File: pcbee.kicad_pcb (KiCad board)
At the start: 2 copper layers, 50.8 x 43.2 mm, 5 parts

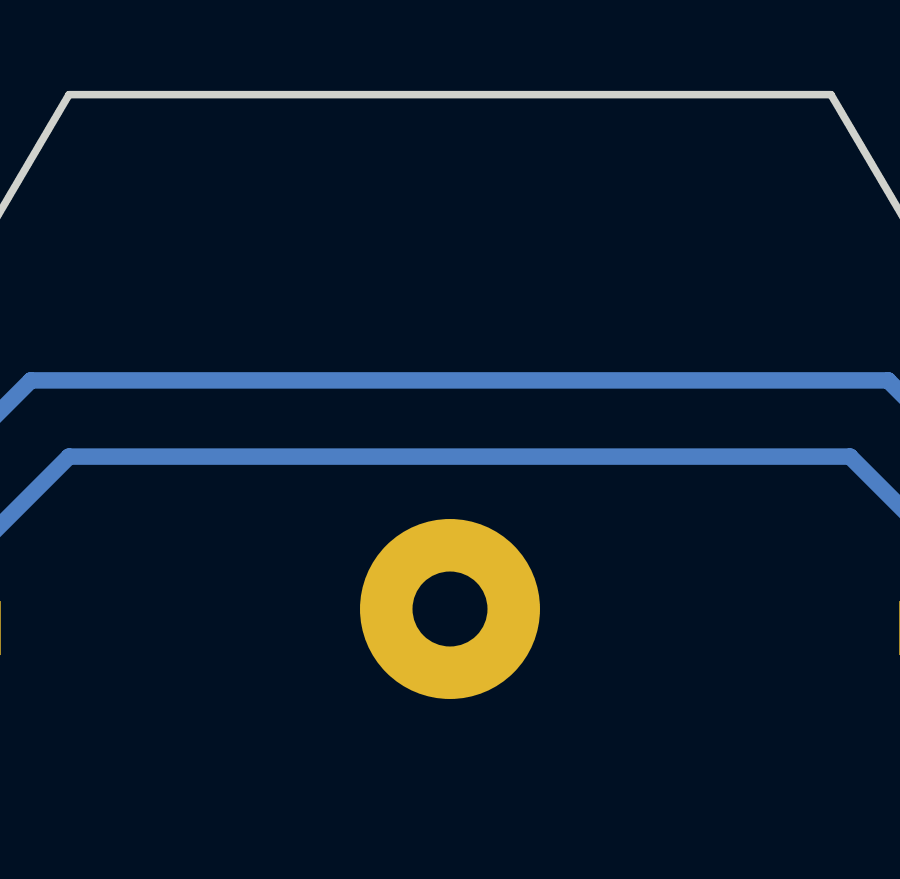
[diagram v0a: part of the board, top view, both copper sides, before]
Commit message: move mounting hole
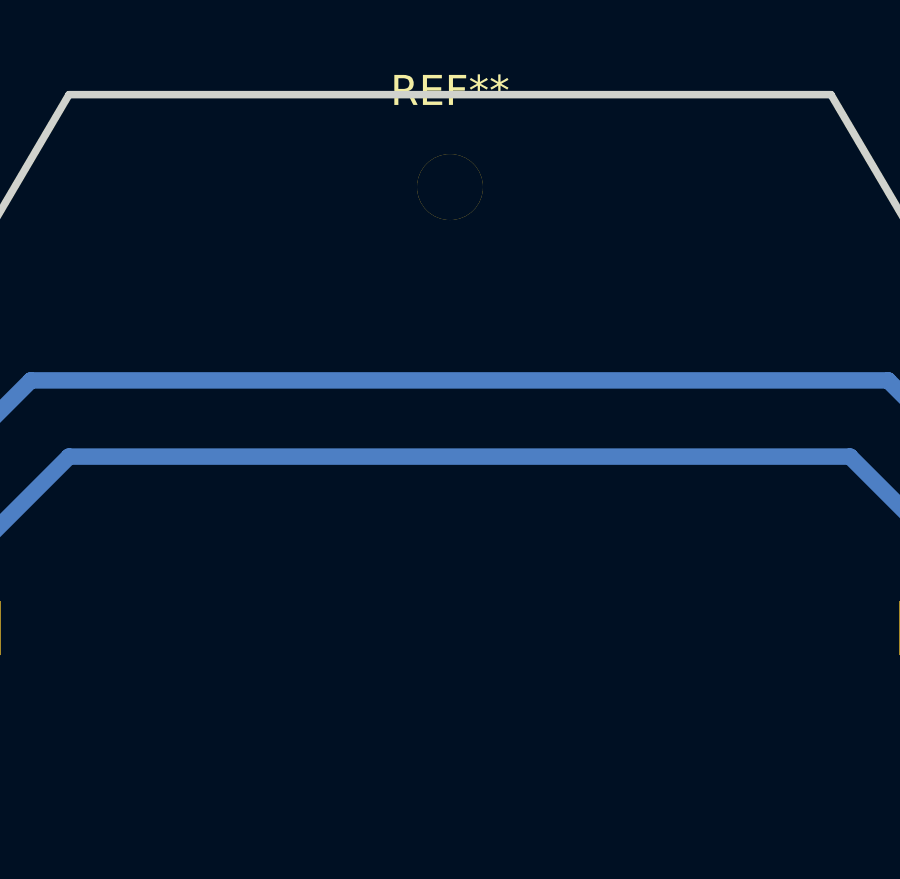
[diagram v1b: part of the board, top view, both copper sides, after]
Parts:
- removed the REF** at (149.9, 92.1)
- added REF**: MountingHole_2.2mm_M2_Pad, Mounting_Holes:MountingHole_2.2mm_M2_Pad, F.Cu at (149.9, 78.0)
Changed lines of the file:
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@@
-(kicad_pcb (version 4) (host pcbnew 4.0.7+dfsg1-1)
+(kicad_pcb (version 4) (host pcbnew 4.0.7)
   (general
     (links 4)
     (no_connects 0)
-    (area 124.334999 74.804999 175.385001 119.485)
+    (area 124.334999 74.804999 175.385001 118.235001)
     (thickness 1.6)
     (drawings 8)
@@
     (34 B.Paste user hide)
     (35 F.Paste user)
-    (36 B.SilkS user hide)
+    (36 B.SilkS user)
     (37 F.SilkS user)
-    (38 B.Mask user hide)
-    (39 F.Mask user hide)
+    (38 B.Mask user)
+    (39 F.Mask user)
     (40 Dwgs.User user hide)
     (41 Cmts.User user hide)
@@
     (mod_text_size 1 1)
     (mod_text_width 0.15)
-    (pad_size 1.524 1.524)
-    (pad_drill 0.762)
+    (pad_size 2.2 2.2)
+    (pad_drill 2.2)
     (pad_to_mask_clearance 0.2)
     (aux_axis_origin 0 0)
-    (visible_elements FFFF3F1F)
+    (visible_elements FFFF7F9F)
     (pcbplotparams
       (layerselection 0x010f0_80000001)
@@
       (xy 0.536977 -4.539402) (xy 0.697932 -4.645079) (xy 0.864099 -4.626846)) (layer F.Mask) (width 0.01))
   )
-  (module Wire_Pads:SolderWirePad_single_2-5mmDrill (layer F.Cu)
-    (at 149.86 92.075)
-    (fp_text reference REF** (at 0 -5.08) (layer F.SilkS) hide
+  (module Mounting_Holes:MountingHole_2.2mm_M2_Pad (layer F.Cu)
+    (at 149.86 78.01)
+    (descr "Mounting Hole 2.2mm, M2")
+    (tags "mounting hole 2.2mm m2")
+    (attr virtual)
+    (fp_text reference REF** (at 0 -3.2) (layer F.SilkS)
       (effects (font (size 1 1) (thickness 0.15)))
     )
-    (fp_text value SolderWirePad_single_2-5mmDrill (at 1.27 5.08) (layer F.Fab)
+    (fp_text value MountingHole_2.2mm_M2_Pad (at 0 3.2) (layer F.Fab)
       (effects (font (size 1 1) (thickness 0.15)))
     )
-    (pad 1 thru_hole circle (at 0 0) (size 5.99948 5.99948) (drill 2.49936) (layers *.Cu *.Mask))
+    (fp_text user %R (at 0.3 0) (layer F.Fab)
+      (effects (font (size 1 1) (thickness 0.15)))
+    )
+    (fp_circle (center 0 0) (end 2.2 0) (layer Cmts.User) (width 0.15))
+    (fp_circle (center 0 0) (end 2.45 0) (layer F.CrtYd) (width 0.05))
+    (pad 1 thru_hole circle (at 0 0) (size 2.2 2.2) (drill 2.2) (layers *.Cu *.Mask))
   )
   (gr_text "PRODUCTION ID\nMUST BE ON\nTHIS (BACK) SILK" (at 150.495 99.695) (layer B.Fab)
     (effects (font (size 1.5 1.5) (thickness 0.3)))
   )
-  (gr_text "Designed by Committee\nat Hackspace Manchester\n2018" (at 149.86 80.01) (layer B.SilkS)
+  (gr_text "Designed by Committee\nat Hackspace Manchester\n2018" (at 149.86 85.01) (layer B.SilkS)
     (effects (font (size 1.2 1.2) (thickness 0.3)) (justify mirror))
   )
